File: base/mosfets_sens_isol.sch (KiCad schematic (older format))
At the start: 81 parts, among them Q1 irf540n, Q2 irf540n, Q3 irf540n, Q4 irf540n, Q5 irf540n, Q6 irf540n, Q7 irf540n, Q8 irf540n, U1 SI8640, U10 ADS7886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

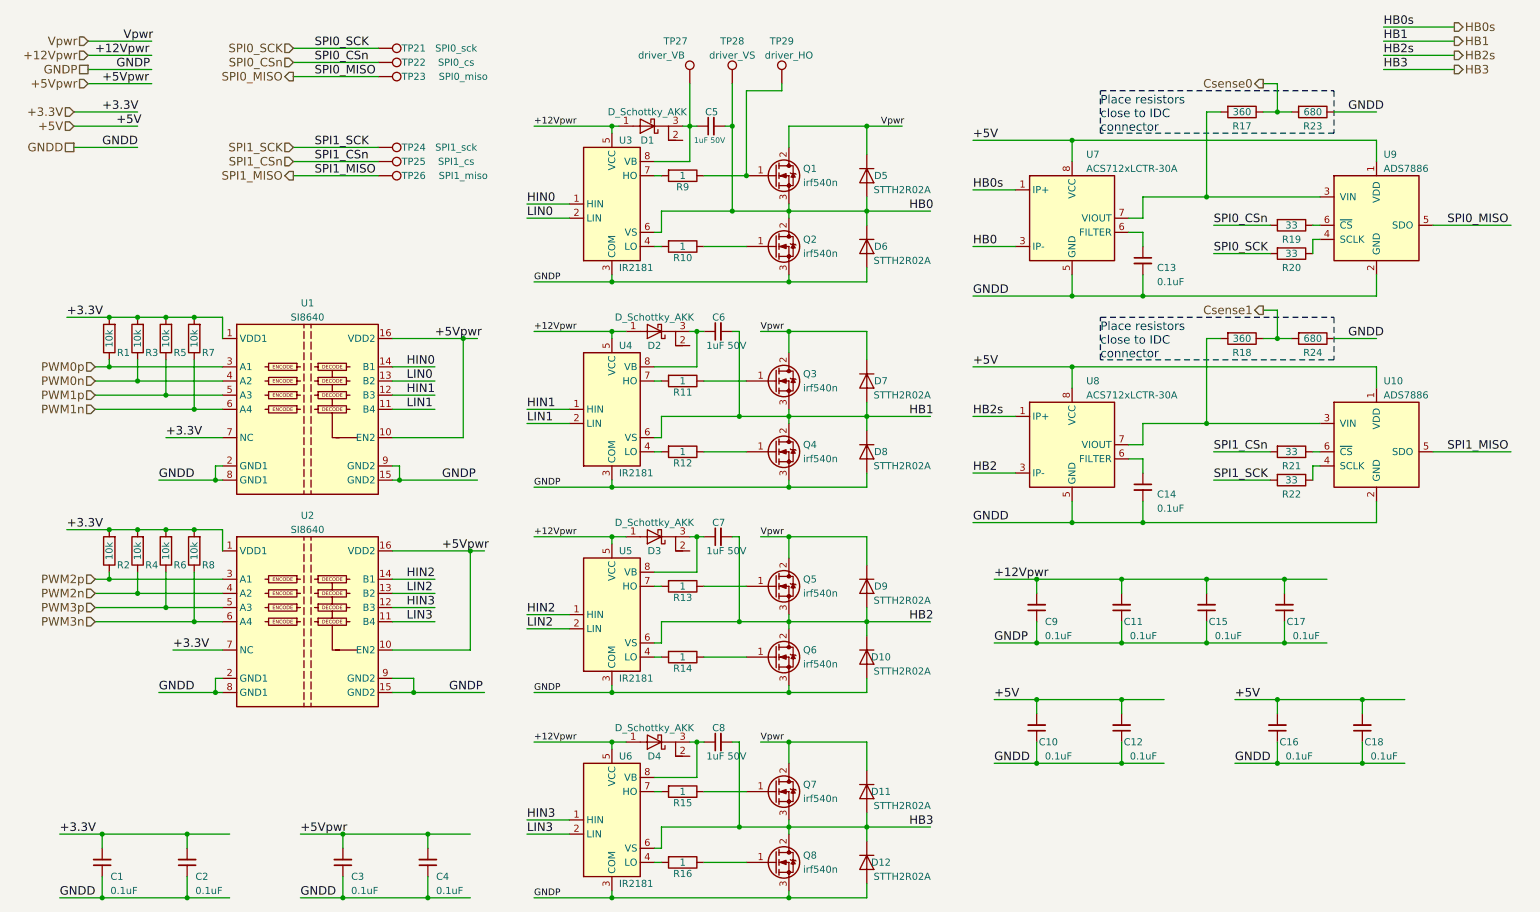
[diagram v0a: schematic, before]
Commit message: upd adc
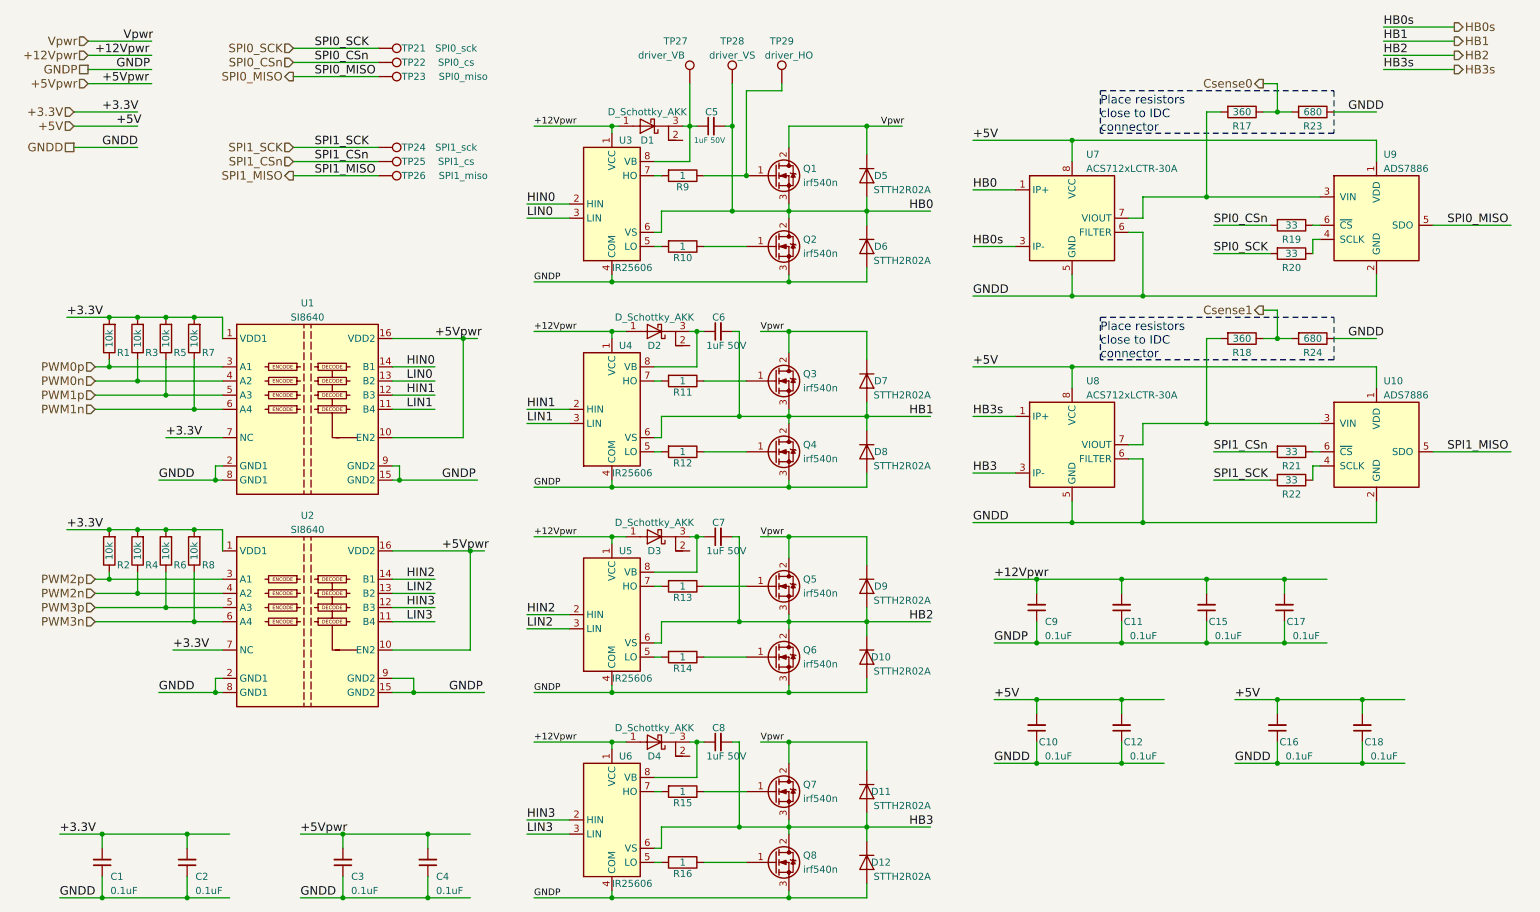
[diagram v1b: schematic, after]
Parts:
- removed C13, C14: 0.1uF, Capacitor_SMD:C_0603_1608Metric, symbol C_Small
- removed U3, U4, U5, U6: IR2181, Package_SOIC:SOIC-8_3.9x4.9mm_P1.27mm, symbol IR2181
- added U3, U4, U5, U6: IR25606, Package_SOIC:SOIC-8_3.9x4.9mm_P1.27mm, symbol IR2101
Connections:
- net labels added: HB3s
- net labels removed: HB2s
- wire segments 254 -> 252
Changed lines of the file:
@@
 HB1
 Text HLabel 10750 800  2    60   Output ~ 0
-HB2s
+HB2
 Text HLabel 10750 900  2    60   Output ~ 0
-HB3
+HB3s
 Text HLabel 1150 3000 0    60   Input ~ 0
 PWM0p
@@
 Vpwr
 $Comp
-L IR2181 U3
-U 1 1 5A1E086C
-P 4800 1850
-F 0 "U3" H 4850 2300 50  0000 L CNN
-F 1 "IR2181" H 4850 1400 50  0000 L CNN
-F 2 "Package_SOIC:SOIC-8_3.9x4.9mm_P1.27mm" H 4800 1850 50  0001 C CIN
-F 3 "" H 4800 1850 50  0001 C CNN
-	1    4800 1850
-	1    0    0    -1
-$EndComp
-$Comp
 L R R9
 U 1 1 5A1E09A7
@@
 $EndComp
 $Comp
-L IR2181 U5
-U 1 1 5A25F65A
-P 4800 4750
-F 0 "U5" H 4850 5200 50  0000 L CNN
-F 1 "IR2181" H 4850 4300 50  0000 L CNN
-F 2 "Package_SOIC:SOIC-8_3.9x4.9mm_P1.27mm" H 4800 4750 50  0001 C CIN
-F 3 "" H 4800 4750 50  0001 C CNN
-	1    4800 4750
-	1    0    0    -1
-$EndComp
-$Comp
 L R R13
 U 1 1 5A25F660
@@
 F 3 "" H 5950 6500 50  0001 C CNN
 	1    5950 6500
-	1    0    0    -1
-$EndComp
-$Comp
-L IR2181 U6
-U 1 1 5A25F6B4
-P 4800 6200
-F 0 "U6" H 4850 6650 50  0000 L CNN
-F 1 "IR2181" H 4850 5750 50  0000 L CNN
-F 2 "Package_SOIC:SOIC-8_3.9x4.9mm_P1.27mm" H 4800 6200 50  0001 C CIN
-F 3 "" H 4800 6200 50  0001 C CNN
-	1    4800 6200
 	1    0    0    -1
 $EndComp
@@
 	1    0    0    -1
 $EndComp
-$Comp
-L C_Small C13
-U 1 1 5A264A9C
-P 8550 2250
-F 0 "C13" H 8650 2200 50  0000 L CNN
-F 1 "0.1uF" H 8650 2100 50  0000 L CNN
-F 2 "Capacitor_SMD:C_0603_1608Metric" H 8550 2250 50  0001 C CNN
-F 3 "" H 8550 2250 50  0001 C CNN
-	1    8550 2250
-	1    0    0    -1
-$EndComp
 Text Label 7350 2500 0    60   ~ 0
 GNDD
@@
 Text Label 6900 1900 0    60   ~ 0
 HB0
+Text Label 7350 1750 0    60   ~ 0
+HB0
 Text Label 7350 2150 0    60   ~ 0
-HB0
-Text Label 7350 1750 0    60   ~ 0
 HB0s
 Text Label 6900 3350 0    60   ~ 0
@@
 HB2
 Text Label 10250 800  0    60   ~ 0
-HB2s
+HB2
 Text Label 10250 600  0    60   ~ 0
 HB0s
@@
 HB3
 Text Label 10250 900  0    60   ~ 0
-HB3
+HB3s
 Text Label 1200 1200 0    60   ~ 0
 +3.3V
@@
 +5V
 Text Label 7350 3350 0    60   ~ 0
-HB2s
+HB3s
 Text Label 7350 3750 0    60   ~ 0
-HB2
+HB3
 Text Label 7350 4100 0    60   ~ 0
 GNDD
-$Comp
-L C_Small C14
-U 1 1 5A254D23
-P 8550 3850
-F 0 "C14" H 8650 3800 50  0000 L CNN
-F 1 "0.1uF" H 8650 3700 50  0000 L CNN
-F 2 "Capacitor_SMD:C_0603_1608Metric" H 8550 3850 50  0001 C CNN
-F 3 "" H 8550 3850 50  0001 C CNN
-	1    8550 3850
-	1    0    0    -1
-$EndComp
 $Comp
 L ACS712xLCTR-30A U8
@@
 Connection ~ 8550 2500
 Wire Wire Line
-	8550 2350 8550 2500
+	8550 2050 8550 2500
 Wire Wire Line
 	8050 2500 8050 2350
-Wire Wire Line
-	8550 2050 8550 2150
 Wire Wire Line
 	8450 2050 8550 2050
@@
 	8450 3650 8550 3650
 Wire Wire Line
-	8550 3650 8550 3750
+	8550 3650 8550 4100
 Wire Wire Line
 	7350 4100 10200 4100
 Wire Wire Line
 	8050 4100 8050 3950
-Wire Wire Line
-	8550 4100 8550 3950
 Connection ~ 8550 4100
 Connection ~ 8050 4100
@@
 Wire Wire Line
 	5350 4200 5450 4200
-$Comp
-L IR2181 U4
-U 1 1 5A25F1D0
-P 4800 3300
-F 0 "U4" H 4850 3750 50  0000 L CNN
-F 1 "IR2181" H 4850 2850 50  0000 L CNN
-F 2 "Package_SOIC:SOIC-8_3.9x4.9mm_P1.27mm" H 4800 3300 50  0001 C CIN
-F 3 "" H 4800 3300 50  0001 C CNN
-	1    4800 3300
-	1    0    0    -1
-$EndComp
 Wire Wire Line
 	4250 2750 4900 2750
@@
 	-1   0    0    1
 $EndComp
+$Comp
+L IR2101 U3
+U 1 1 5A8A38B7
+P 4800 1850
+F 0 "U3" H 4850 2300 50  0000 L CNN
+F 1 "IR25606" H 4800 1400 50  0000 L CNN
+F 2 "Package_SOIC:SOIC-8_3.9x4.9mm_P1.27mm" H 4800 1850 50  0001 C CIN
+F 3 "" H 4800 1850 50  0001 C CNN
+	1    4800 1850
+	1    0    0    -1
+$EndComp
+$Comp
+L IR2101 U4
+U 1 1 5A8A46BA
+P 4800 3300
+F 0 "U4" H 4850 3750 50  0000 L CNN
+F 1 "IR25606" H 4800 2850 50  0000 L CNN
+F 2 "Package_SOIC:SOIC-8_3.9x4.9mm_P1.27mm" H 4800 3300 50  0001 C CIN
+F 3 "" H 4800 3300 50  0001 C CNN
+	1    4800 3300
+	1    0    0    -1
+$EndComp
+$Comp
+L IR2101 U5
+U 1 1 5A8A4DFF
+P 4800 4750
+F 0 "U5" H 4850 5200 50  0000 L CNN
+F 1 "IR25606" H 4800 4300 50  0000 L CNN
+F 2 "Package_SOIC:SOIC-8_3.9x4.9mm_P1.27mm" H 4800 4750 50  0001 C CIN
+F 3 "" H 4800 4750 50  0001 C CNN
+	1    4800 4750
+	1    0    0    -1
+$EndComp
+$Comp
+L IR2101 U6
+U 1 1 5A8A501E
+P 4800 6200
+F 0 "U6" H 4850 6650 50  0000 L CNN
+F 1 "IR25606" H 4800 5750 50  0000 L CNN
+F 2 "Package_SOIC:SOIC-8_3.9x4.9mm_P1.27mm" H 4800 6200 50  0001 C CIN
+F 3 "" H 4800 6200 50  0001 C CNN
+	1    4800 6200
+	1    0    0    -1
+$EndComp
 $EndSCHEMATC

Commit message: upd
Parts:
- renumbered C15 to C13, C16 to C14, C17 to C15, C18 to C16
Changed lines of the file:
@@
 $EndComp
 $Comp
-L C_Small C15
+L C_Small C13
 U 1 1 5A259095
 P 9000 4700
-F 0 "C15" H 8850 4800 50  0000 L CNN
+F 0 "C13" H 8850 4800 50  0000 L CNN
 F 1 "0.1uF" H 8750 4900 50  0000 L CNN
 F 2 "Capacitor_SMD:C_0603_1608Metric" H 9000 4700 50  0001 C CNN
@@
 $EndComp
 $Comp
-L C_Small C17
+L C_Small C15
 U 1 1 5A2593B9
 P 9550 4700
-F 0 "C17" H 9400 4800 50  0000 L CNN
+F 0 "C15" H 9400 4800 50  0000 L CNN
 F 1 "0.1uF" H 9300 4900 50  0000 L CNN
 F 2 "Capacitor_SMD:C_0603_1608Metric" H 9550 4700 50  0001 C CNN
@@
 $EndComp
 $Comp
-L C_Small C16
+L C_Small C14
 U 1 1 5A25BF04
 P 9500 5550
-F 0 "C16" H 9350 5650 50  0000 L CNN
+F 0 "C14" H 9350 5650 50  0000 L CNN
 F 1 "0.1uF" H 9250 5750 50  0000 L CNN
 F 2 "Capacitor_SMD:C_0603_1608Metric" H 9500 5550 50  0001 C CNN
@@
 $EndComp
 $Comp
-L C_Small C18
+L C_Small C16
 U 1 1 5A25BF0A
 P 10100 5550
-F 0 "C18" H 9950 5650 50  0000 L CNN
+F 0 "C16" H 9950 5650 50  0000 L CNN
 F 1 "0.1uF" H 9850 5750 50  0000 L CNN
 F 2 "Capacitor_SMD:C_0603_1608Metric" H 10100 5550 50  0001 C CNN

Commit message: upd
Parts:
- removed C14, C16: 0.1uF, Capacitor_SMD:C_0603_1608Metric, symbol C_Small
- removed R19, R20, R21, R22: 33, Resistor_SMD:R_0603_1608Metric, symbol R
- removed TP21: SPI0_sck, TestPoint:TestPoint_Pad_D1.5mm, symbol Test_Point
- removed TP22: SPI0_cs, TestPoint:TestPoint_Pad_D1.5mm, symbol Test_Point
- removed TP23: SPI0_miso, TestPoint:TestPoint_Pad_D1.5mm, symbol Test_Point
- removed TP24: SPI1_sck, TestPoint:TestPoint_Pad_D1.5mm, symbol Test_Point
- removed TP25: SPI1_cs, TestPoint:TestPoint_Pad_D1.5mm, symbol Test_Point
- removed TP26: SPI1_miso, TestPoint:TestPoint_Pad_D1.5mm, symbol Test_Point
- removed U10, U9: ADS7886, Package_TO_SOT_SMD:SOT-23-6, symbol ADS7886
- added C14, C16: CP, Capacitor_THT:CP_Radial_D22.0mm_P10.00mm_SnapIn, symbol CP
- added C40, C41, C48, C49: CP, Capacitor_THT:CP_Radial_D10.0mm_P5.00mm, symbol CP
- added C42, C43: CP, Capacitor_THT:CP_Radial_D12.5mm_P5.00mm, symbol CP
- added C44, C45, C46, C47: CP, Capacitor_SMD:C_2220_5650Metric_Pad2.02x5.50mm_HandSolder, symbol CP
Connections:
- net labels removed: SPI0_CSn, SPI0_MISO, SPI0_SCK, SPI1_CSn, SPI1_MISO, SPI1_SCK
- wire segments 252 -> 254

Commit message: current version
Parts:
- removed TP27: driver_VB, TestPoint:TestPoint_Pad_D1.5mm, symbol Test_Point
- removed TP28: driver_VS, TestPoint:TestPoint_Pad_D1.5mm, symbol Test_Point
- removed TP29: driver_HO, TestPoint:TestPoint_Pad_D1.5mm, symbol Test_Point
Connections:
- wire segments 254 -> 251
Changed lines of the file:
@@
 Text Notes 8250 2950 0    60   ~ 0
 Place resistors\nclose to IDC\nconnector
-$Comp
-L Test_Point TP28
-U 1 1 5A4A934F
-P 5650 1000
-F 0 "TP28" H 5650 1300 50  0000 C CNN
-F 1 "driver_VS" H 5650 1200 50  0000 C CNN
-F 2 "TestPoint:TestPoint_Pad_D1.5mm" H 5850 1000 50  0001 C CNN
-F 3 "" H 5850 1000 50  0001 C CNN
-	1    5650 1000
-	1    0    0    -1
-$EndComp
-$Comp
-L Test_Point TP27
-U 1 1 5A4A9424
-P 5350 1000
-F 0 "TP27" H 5250 1300 50  0000 C CNN
-F 1 "driver_VB" H 5150 1200 50  0000 C CNN
-F 2 "TestPoint:TestPoint_Pad_D1.5mm" H 5550 1000 50  0001 C CNN
-F 3 "" H 5550 1000 50  0001 C CNN
-	1    5350 1000
-	1    0    0    -1
-$EndComp
-$Comp
-L Test_Point TP29
-U 1 1 5A4AA2DB
-P 6000 1000
-F 0 "TP29" H 6000 1300 50  0000 C CNN
-F 1 "driver_HO" H 6050 1200 50  0000 C CNN
-F 2 "TestPoint:TestPoint_Pad_D1.5mm" H 6200 1000 50  0001 C CNN
-F 3 "" H 6200 1000 50  0001 C CNN
-	1    6000 1000
-	1    0    0    -1
-$EndComp
 Wire Wire Line
 	3250 5200 3400 5200
@@
 	6050 1300 6850 1300
 Connection ~ 5650 1900
-Wire Wire Line
-	5650 1000 5650 1900
 Wire Wire Line
 	5600 1300 5650 1300
@@
 Connection ~ 5750 1650
 Connection ~ 6600 1300
-Wire Wire Line
-	5750 1650 5750 1050
-Wire Wire Line
-	5750 1050 6000 1050
-Wire Wire Line
-	6000 1050 6000 1000
 $Comp
 L D_Schottky_AKK D1
@@
 Text Label 7500 5350 0    60   ~ 0
 +3.3V
+Wire Wire Line
+	5650 1000 5650 1900
 $EndSCHEMATC
